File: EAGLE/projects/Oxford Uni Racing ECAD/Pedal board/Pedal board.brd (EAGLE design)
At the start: 160 x 202.9 mm, 27 parts, among them J1 T821108A1S100CEU, K1 RT444012, T1 BT169

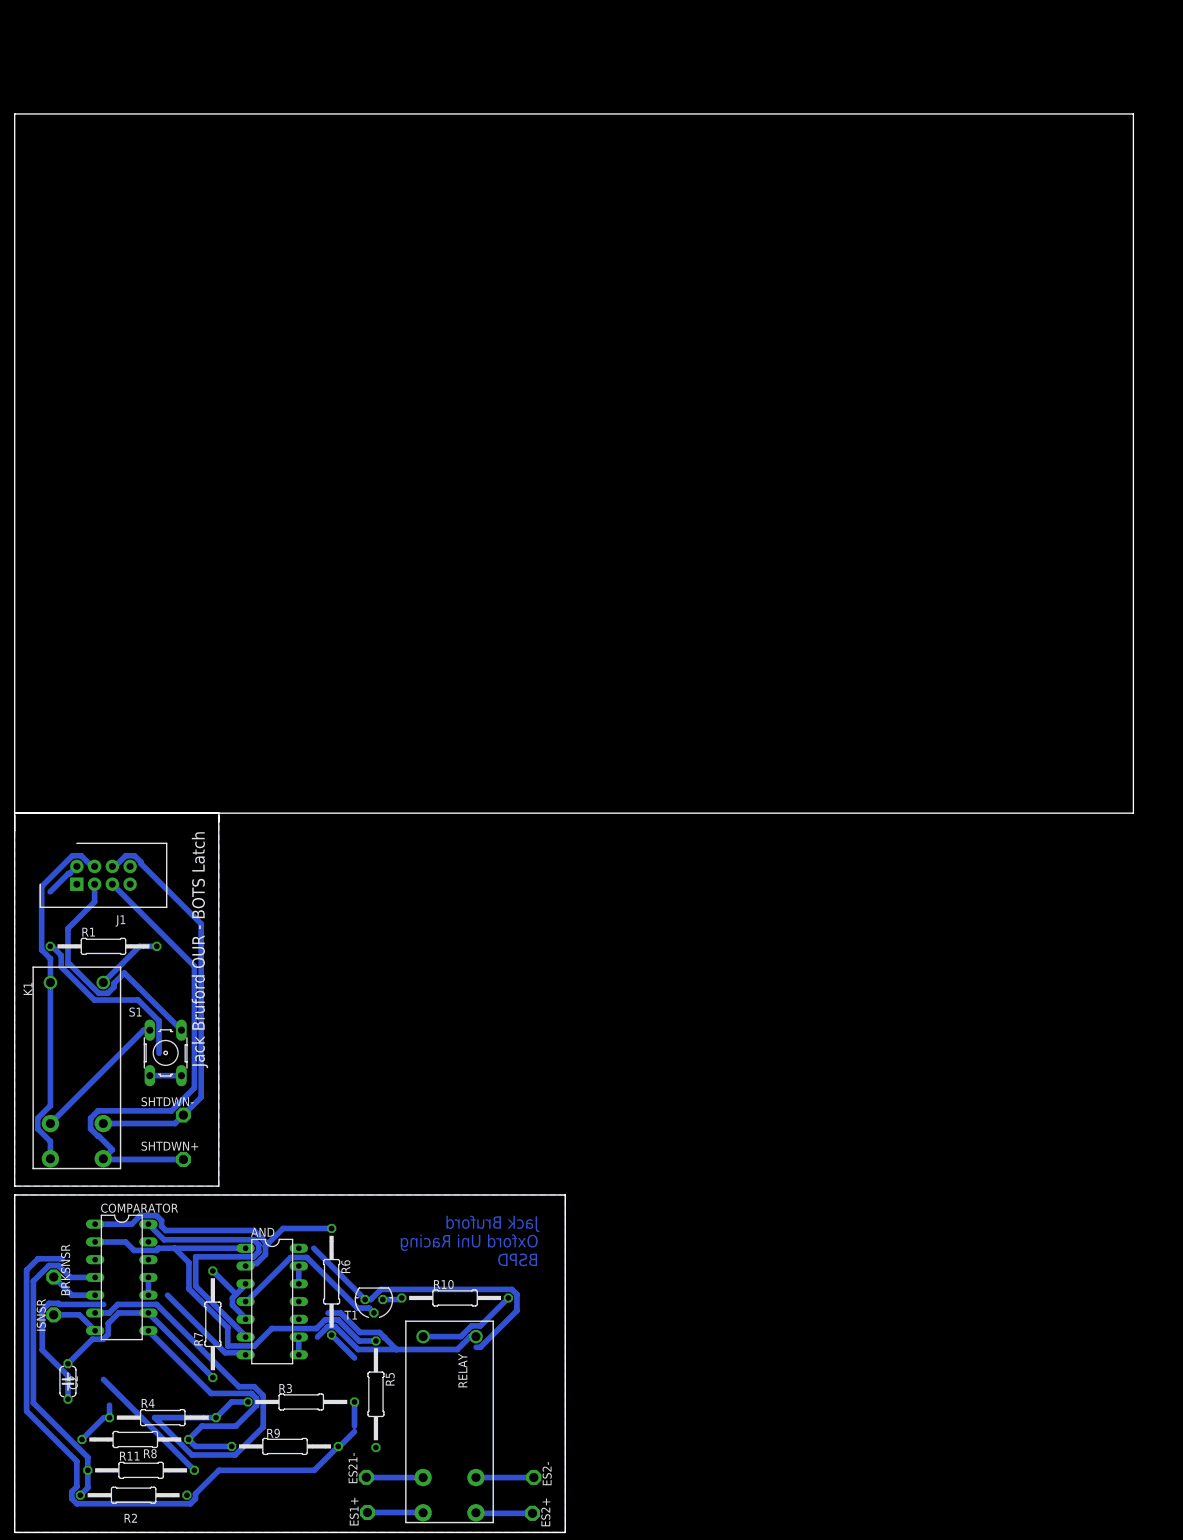
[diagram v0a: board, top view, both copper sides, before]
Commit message: added can connector to pedal board, updated descriprion to power delivery
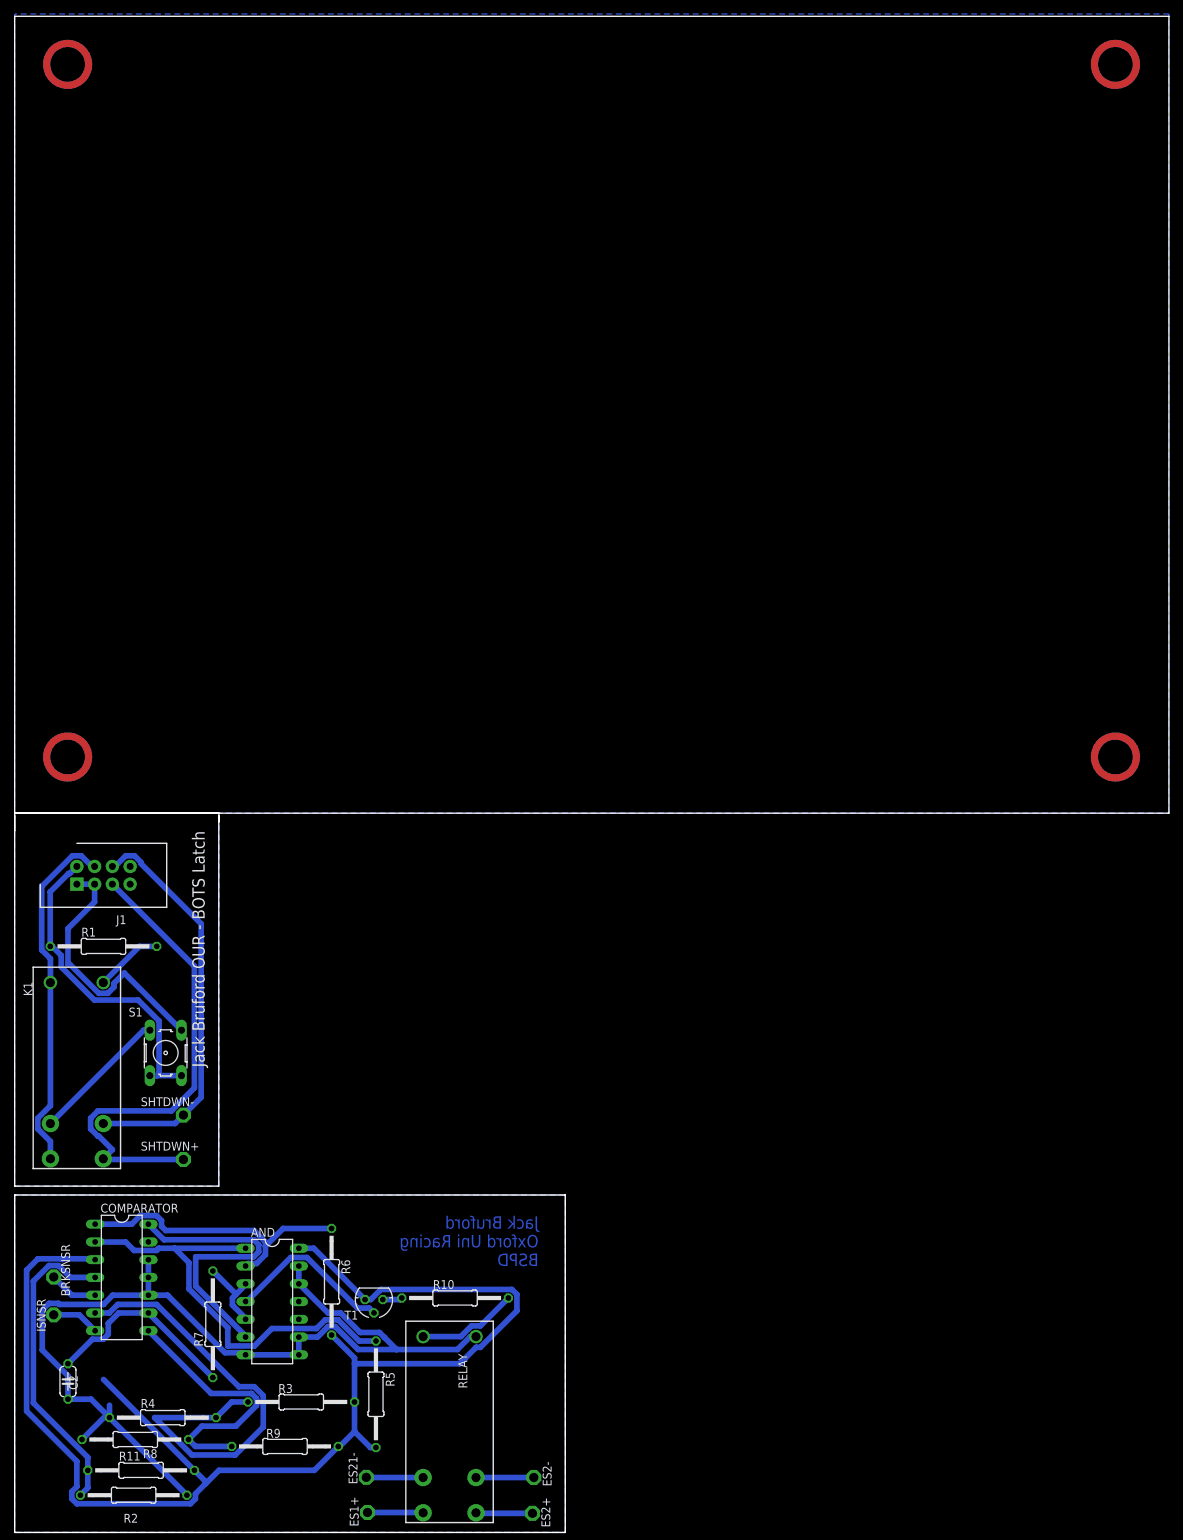
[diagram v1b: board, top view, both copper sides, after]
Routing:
- net GND: track 125.0 -> 187.4 mm
- net 12V: track 192.9 -> 234.5 mm
- added copper zone on layer 16, net GND2
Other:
- board size 160 x 202.9 mm -> 165.1 x 216.8 mm

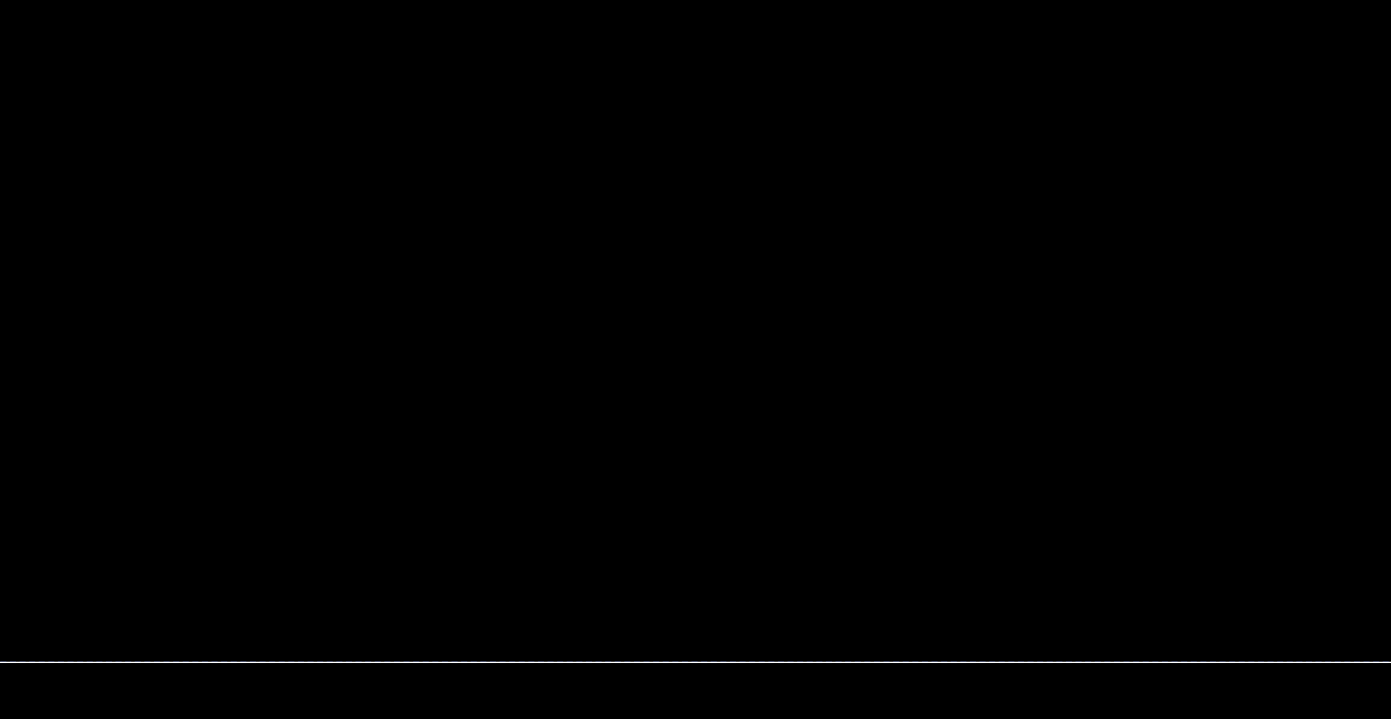
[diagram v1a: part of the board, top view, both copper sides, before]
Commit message: added power delivery to pedal board
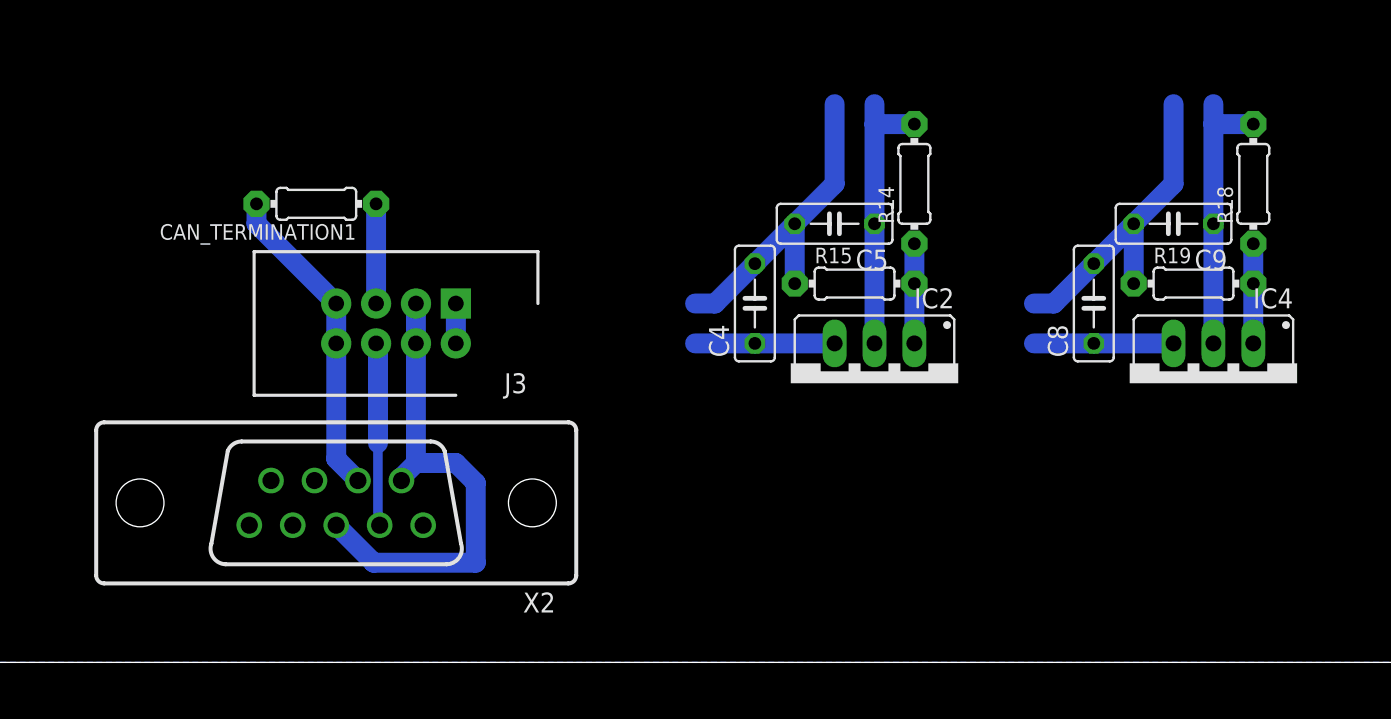
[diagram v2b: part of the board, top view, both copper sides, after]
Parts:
- added C4, C8: 0.1uF, adafruit:C050-025X075
- added C5, C9: 1uF, adafruit:C050-025X075
- added CAN_TERMINATION1: 120, adafruit:0204/7
- added IC2, IC4: (no value), v-reg:317TS
- added J3: T821108A1S100CEU, T821108A1S100CEU:HDRV8W64P254_2X4_1778X895X915P
- added R14, R18: 240, adafruit:0204/7
- added R15: 390, adafruit:0204/7
- added R19: 720, adafruit:0204/7
- added X2: D-SUB9-H2M09ST, con-thomas-betts:H2M09ST
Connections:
- new net 5V: C5.1, C9.1, IC2.2, IC4.2, R14.2, R18.2, X2.9
- new net CAN_H: CAN_TERMINATION1.2, J3.7, J3.8, X2.7
- new net CAN_L: CAN_TERMINATION1.1, J3.5, J3.6, X2.2
- new net N$24: IC2.1, R14.1, R15.2
- new net N$26: IC4.1, R18.1, R19.2
- net 12V: now also C4.1, C8.1, IC2.3, IC4.3, J3.1, J3.2
- net GND: now also C4.2, C5.2, C8.2, C9.2, J3.3, J3.4, R15.1, R19.1, X2.3, X2.6
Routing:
- net GND: track 187.4 -> 260.2 mm
- net 5V: track 0.00 -> 35.6 mm
- net 12V: track 234.5 -> 254.8 mm
- net CAN_H: track 0.00 -> 20.3 mm
- net CAN_L: track 0.00 -> 18.9 mm
- net N$26: track 0.00 -> 6.35 mm
- net N$24: track 0.00 -> 6.35 mm
- removed copper zone on layer 16, net GND2

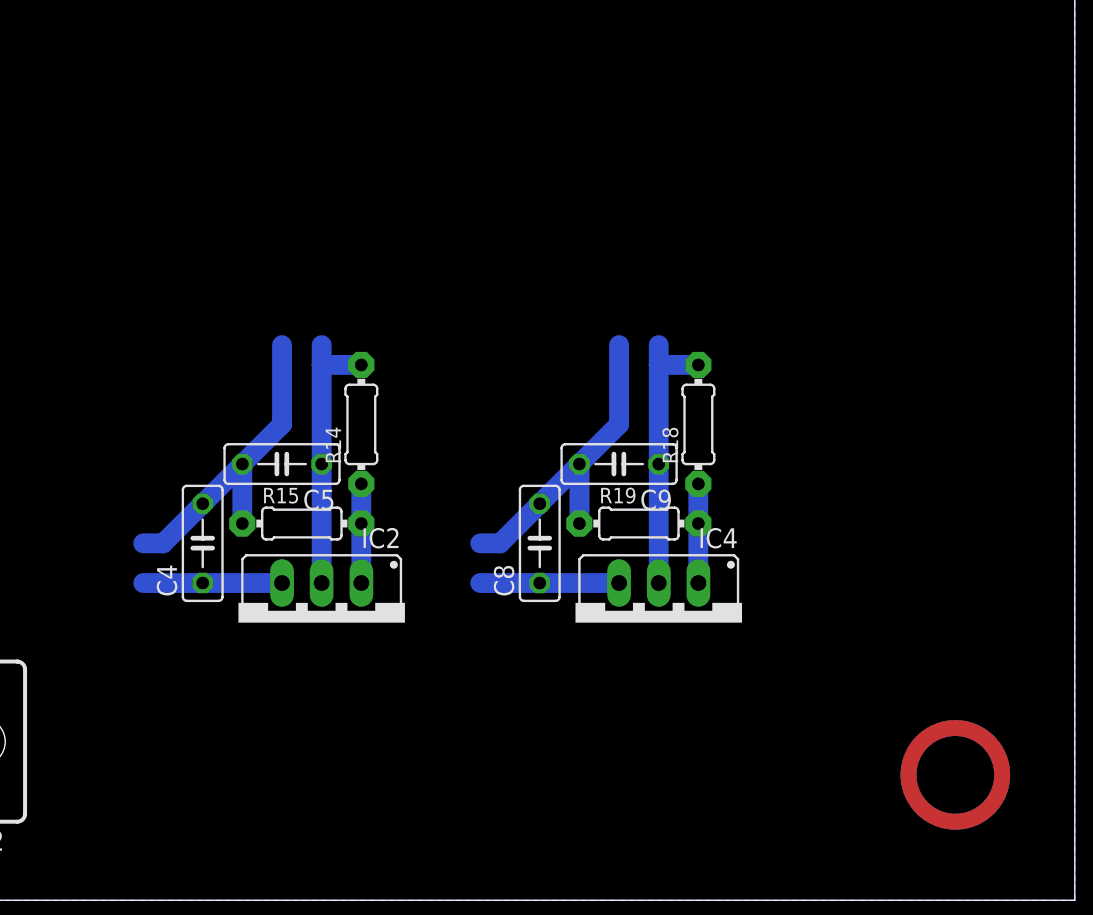
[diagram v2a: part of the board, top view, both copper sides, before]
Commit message: added throttle connectors
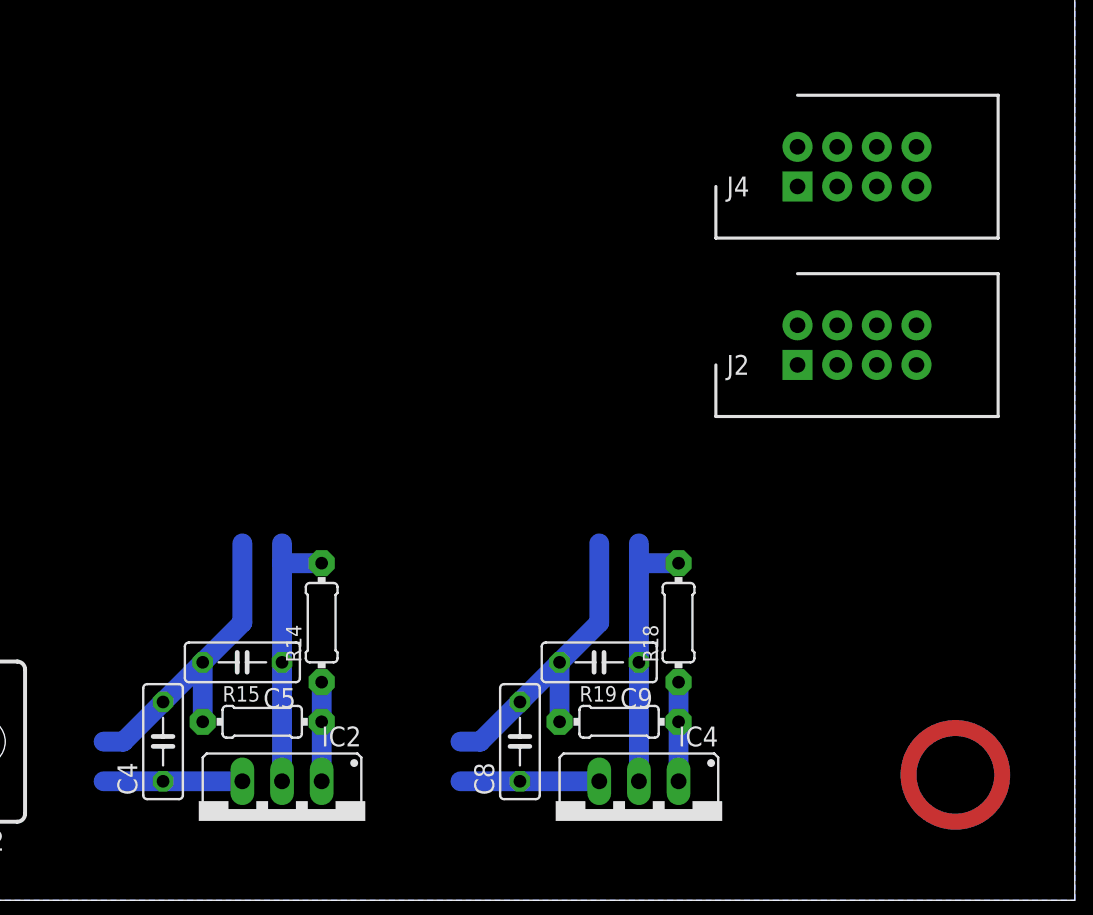
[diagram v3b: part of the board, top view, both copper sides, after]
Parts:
- added J2, J4: T821108A1S100CEU, T821108A1S100CEU:HDRV8W64P254_2X4_1778X895X915P
- moved IC2 13.0 mm to (114.3, 5.08)
- moved C5 13.0 mm to (111.8, 15.2)
- moved C4 13.0 mm to (106.7, 10.2)
- moved R14 13.0 mm to (116.8, 17.8)
- moved R15 13.0 mm to (113.0, 11.4)
- moved IC4 12.8 mm to (137.2, 5.08)
- moved C8 12.8 mm to (129.5, 10.2)
- moved R18 12.8 mm to (139.7, 17.8)
- moved R19 12.8 mm to (135.9, 11.4)
- moved C9 12.8 mm to (134.6, 15.2)
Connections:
- new net 3.3V: C5.1, IC2.2, J2.1, J2.2, J4.1, R14.2
- new net THR1: J2.5
- new net THR2: J2.6
- new net THR3: J4.5
- net 5V: no longer C5.1, IC2.2, R14.2
- net GND: now also J2.3, J2.4, J4.3
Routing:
- net 3.3V: track 0.00 -> 17.8 mm
- net 5V: track 35.6 -> 17.8 mm
